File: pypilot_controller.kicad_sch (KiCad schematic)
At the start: 29 parts, among them J1 power+, J2 power-, J3 power+, J4 power+, Q1 Q_NMOS_GDS, Q2 Q_NMOS_GDS, Q3 Q_NMOS_GDS, Q4 Q_NMOS_GDS, Q5 Q_NMOS_GDS, U2 IR2101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

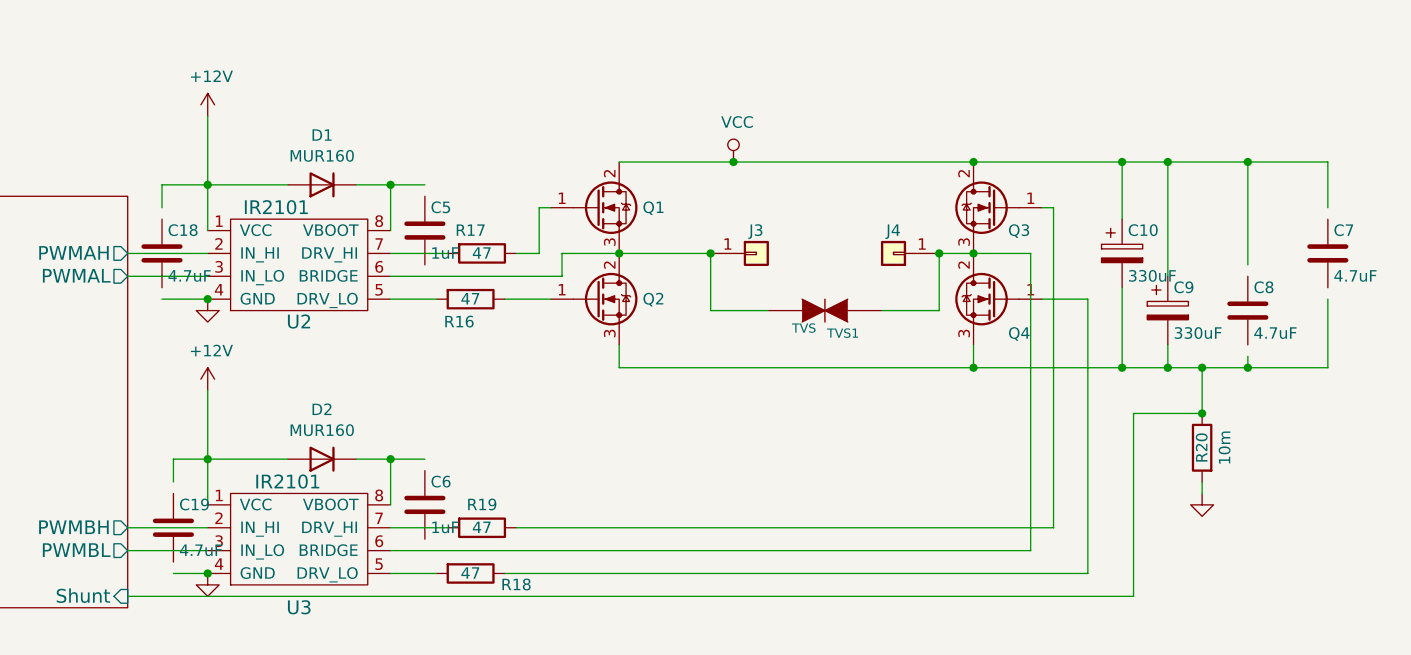
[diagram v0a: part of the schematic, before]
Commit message: Reconnect caps
Stock symbols are smaller than the Freetronics ones were
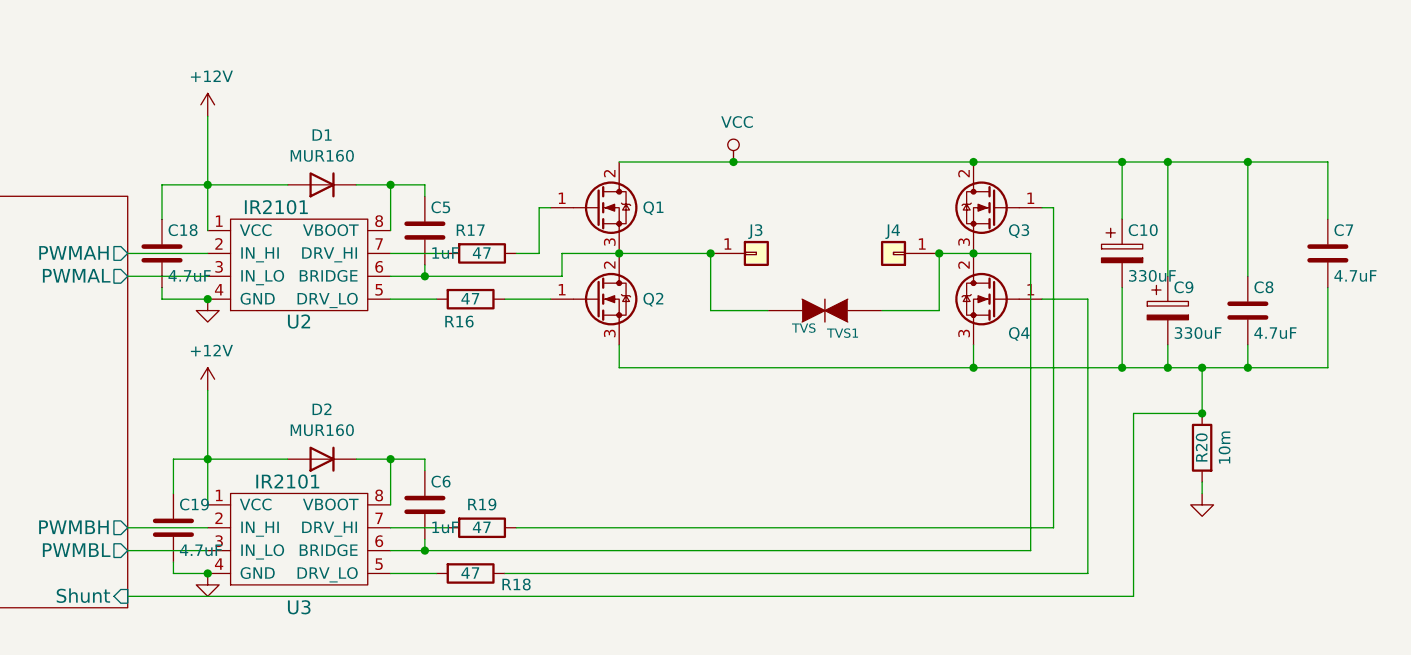
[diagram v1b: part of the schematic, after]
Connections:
- net +12V: now also C18.1, C19.1, C7.1, C8.1
- net GND: now also C18.2, C19.2
- net sense/Shunt: now also C7.2, C8.2
- net at J4.1 (Pin_1), Q3.3 (S), Q4.2 (D)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: now also C6.2
- net at J3.1 (Pin_1), Q1.3 (S), Q2.2 (D)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: now also C5.2
- net at D1.1 (K), U2.8 (VBOOT): now also C5.1
- net at D2.1 (K), U3.8 (VBOOT): now also C6.1
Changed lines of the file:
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@@
+	)
+	(junction
+		(at 152.4 113.03)
+		(diameter 0)
+		(color 0 0 0 0)
 	)
 	(junction
@@
 	)
 	(junction
+		(at 152.4 82.55)
+		(diameter 0)
+		(color 0 0 0 0)
+	)
+	(junction
 		(at 213.36 80.01)
 		(diameter 0)
@@
 	(wire
 		(pts
-			(xy 124.46 105.41) (xy 124.46 102.87)
+			(xy 124.46 102.87) (xy 124.46 106.68)
 		)
 		(stroke
@@
 	(wire
 		(pts
+			(xy 123.19 83.82) (xy 123.19 85.09)
+		)
+		(stroke
+			(width 0)
+			(type default)
+		)
+	)
+	(wire
+		(pts
 			(xy 50.8 30.48) (xy 57.15 30.48)
 		)
@@
 	(wire
 		(pts
+			(xy 252.73 83.82) (xy 252.73 92.71)
+		)
+		(stroke
+			(width 0)
+			(type default)
+		)
+	)
+	(wire
+		(pts
 			(xy 148.59 110.49) (xy 154.94 110.49)
 		)
@@
 	(wire
 		(pts
+			(xy 152.4 113.03) (xy 219.71 113.03)
+		)
+		(stroke
+			(width 0)
+			(type default)
+		)
+	)
+	(wire
+		(pts
 			(xy 124.46 115.57) (xy 128.27 115.57)
 		)
@@
 	(wire
 		(pts
-			(xy 252.73 74.93) (xy 252.73 69.85)
+			(xy 152.4 82.55) (xy 167.64 82.55)
+		)
+		(stroke
+			(width 0)
+			(type default)
+		)
+	)
+	(wire
+		(pts
+			(xy 252.73 69.85) (xy 252.73 76.2)
 		)
 		(stroke
@@
 	(wire
 		(pts
-			(xy 243.84 91.44) (xy 243.84 92.71)
+			(xy 243.84 90.17) (xy 243.84 92.71)
 		)
 		(stroke
@@
 	(wire
 		(pts
+			(xy 152.4 81.28) (xy 152.4 82.55)
+		)
+		(stroke
+			(width 0)
+			(type default)
+		)
+	)
+	(wire
+		(pts
 			(xy 60.96 90.17) (xy 63.5 90.17)
 		)
@@
 	(wire
 		(pts
-			(xy 148.59 113.03) (xy 219.71 113.03)
+			(xy 148.59 113.03) (xy 152.4 113.03)
 		)
 		(stroke
@@
 	(wire
 		(pts
+			(xy 152.4 102.87) (xy 152.4 104.14)
+		)
+		(stroke
+			(width 0)
+			(type default)
+		)
+	)
+	(wire
+		(pts
 			(xy 119.38 118.11) (xy 231.14 118.11)
 		)
@@
 	(wire
 		(pts
-			(xy 123.19 74.93) (xy 123.19 72.39)
+			(xy 123.19 72.39) (xy 123.19 76.2)
 		)
 		(stroke
@@
 	(wire
 		(pts
-			(xy 252.73 85.09) (xy 252.73 92.71)
-		)
-		(stroke
-			(width 0)
-			(type default)
-		)
-	)
-	(wire
-		(pts
 			(xy 50.8 57.15) (xy 50.8 49.53)
 		)
@@
 	(wire
 		(pts
-			(xy 148.59 82.55) (xy 167.64 82.55)
+			(xy 152.4 72.39) (xy 152.4 73.66)
+		)
+		(stroke
+			(width 0)
+			(type default)
+		)
+	)
+	(wire
+		(pts
+			(xy 148.59 82.55) (xy 152.4 82.55)
+		)
+		(stroke
+			(width 0)
+			(type default)
+		)
+	)
+	(wire
+		(pts
+			(xy 152.4 111.76) (xy 152.4 113.03)
 		)
 		(stroke
@@
 	(wire
 		(pts
-			(xy 243.84 81.28) (xy 243.84 69.85)
-		)
-		(stroke
+			(xy 243.84 69.85) (xy 243.84 82.55)
+		)
+		(stroke
+			(width 0)
+			(type default)
+		)
+	)
+	(wire
+		(pts
+			(xy 124.46 114.3) (xy 124.46 115.57)
+		)
+		(stroke

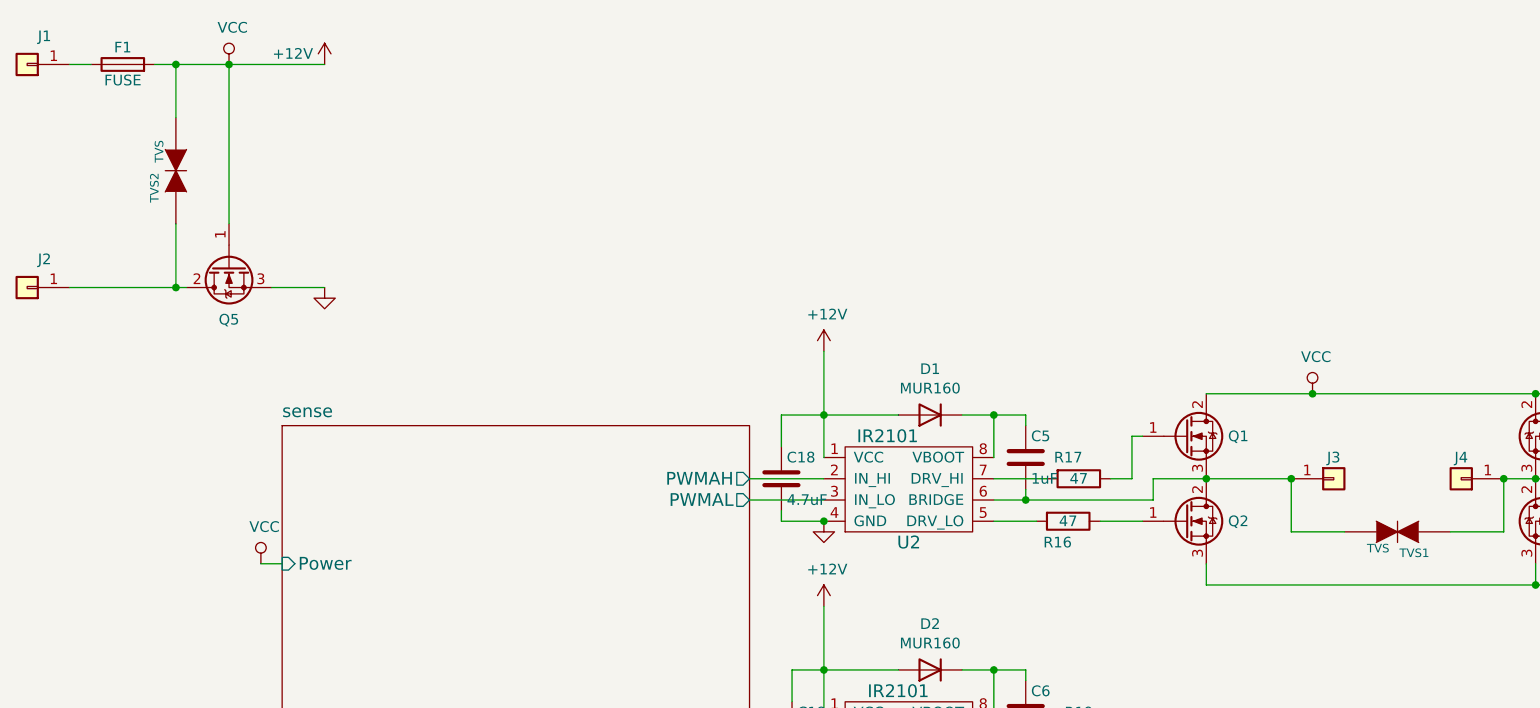
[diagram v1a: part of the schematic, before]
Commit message: Patch in particular TVS model numbers
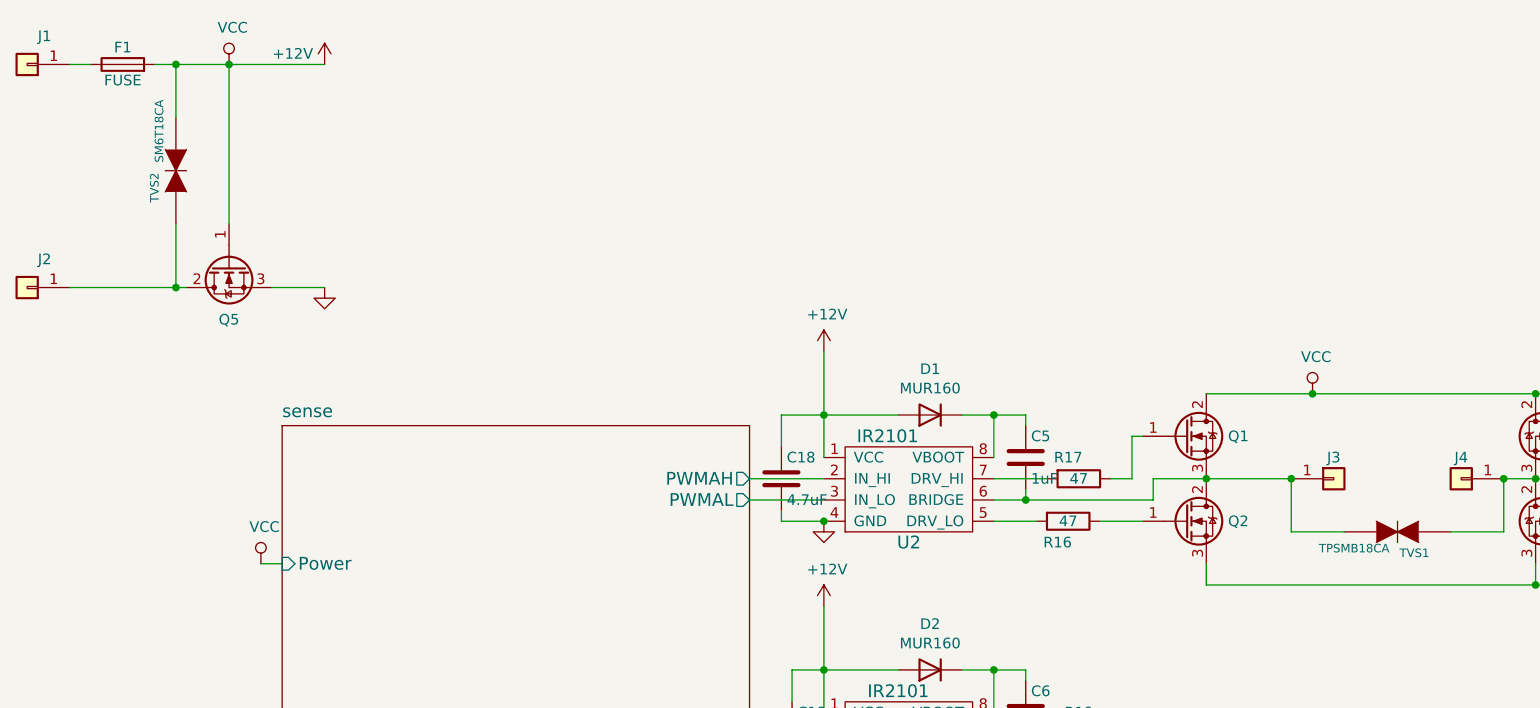
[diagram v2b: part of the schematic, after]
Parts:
- TVS1: value TVS -> TPSMB18CA
- TVS2: value TVS -> SM6T18CA
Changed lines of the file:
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@@
 			)
 		)
-		(property "Value" "TVS"
+		(property "Value" "TPSMB18CA"
 			(at 195.8848 88.3412 0)
 			(effects
@@
 			)
 		)
-		(property "Value" "TVS"
+		(property "Value" "SM6T18CA"
 			(at 48.8188 42.2148 0)
 			(effects

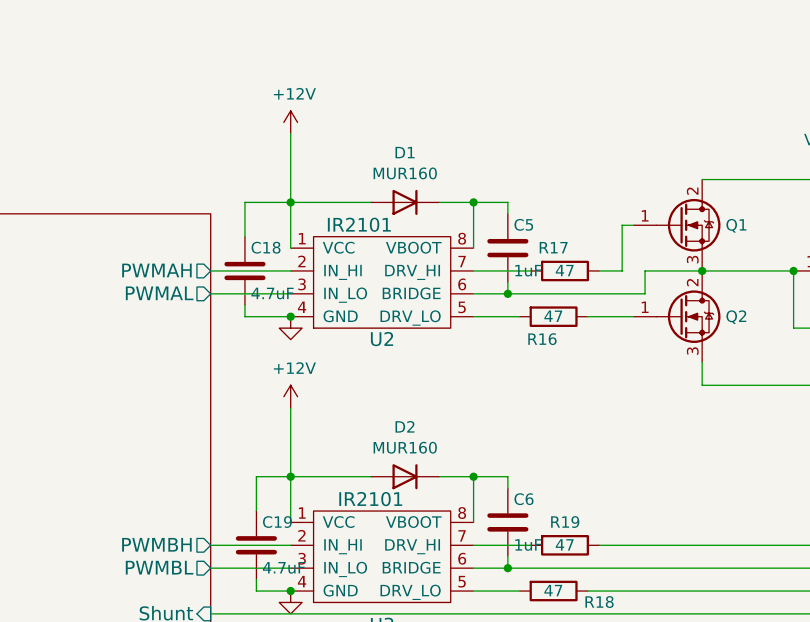
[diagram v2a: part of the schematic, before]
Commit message: Switch the charge pump diode symbol that's actually being used
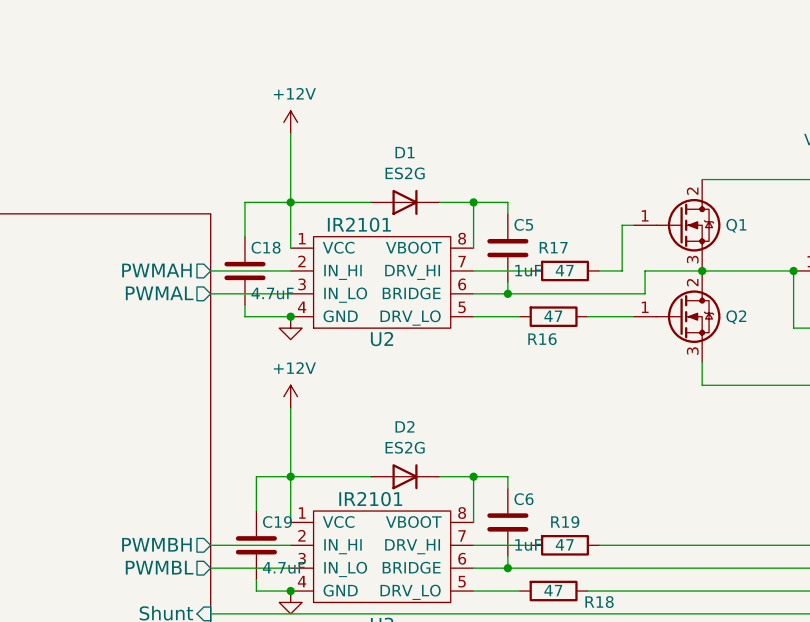
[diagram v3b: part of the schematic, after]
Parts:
- D1, D2: value MUR160 -> ES2G; symbol Diode:1N4001 -> pypilot_components:ES2G
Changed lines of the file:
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@@
 	)
 	(symbol
-		(lib_id "Diode:1N4001")
+		(lib_id "pypilot_components:ES2G")
 		(at 140.97 72.39 180)
 		(unit 1)
@@
 			)
 		)
-		(property "Value" "MUR160"
+		(property "Value" "ES2G"
 			(at 140.97 69.215 0)
 			(effects
@@
 			)
 		)
-		(property "Datasheet" "http://www.vishay.com/docs/88503/1n4001.pdf"
+		(property "Datasheet" "https://www.lcsc.com/datasheet/lcsc_datasheet_2408051407_GOODWORK-ES2G_C2848675.pdf"
 			(at 140.97 72.39 0)
 			(effects
@@
 			)
 		)
-		(property "Description" ""
+		(property "Description" "400V 2A 1.25V@6A fast recovery / high efficiency diode, SMA(DO-214AC)"
 			(at 140.97 72.39 0)
 			(effects
@@
 		)
 		(property "LCSC" "C2848675"
+			(at 140.97 72.39 0)
+			(effects
+				(font
+					(size 1.27 1.27)
+				)
+				(hide yes)
+			)
+		)
+		(property "Sim.Device" "D"
+			(at 140.97 72.39 0)
+			(effects
+				(font
+					(size 1.27 1.27)
+				)
+				(hide yes)
+			)
+		)
+		(property "Sim.Pins" "1=K 2=A"
 			(at 140.97 72.39 0)
 			(effects
@@
 	)
 	(symbol
-		(lib_id "Diode:1N4001")
+		(lib_id "pypilot_components:ES2G")
 		(at 140.97 102.87 180)
 		(unit 1)
@@
 			)
 		)
-		(property "Value" "MUR160"
+		(property "Value" "ES2G"
 			(at 140.97 99.695 0)
 			(effects
@@
 			)
 		)
-		(property "Datasheet" "http://www.vishay.com/docs/88503/1n4001.pdf"
+		(property "Datasheet" "https://www.lcsc.com/datasheet/lcsc_datasheet_2408051407_GOODWORK-ES2G_C2848675.pdf"
 			(at 140.97 102.87 0)
 			(effects
@@
 			)
 		)
-		(property "Description" ""
+		(property "Description" "400V 2A 1.25V@6A fast recovery / high efficiency diode, SMA(DO-214AC)"
 			(at 140.97 102.87 0)
 			(effects
@@
 			(at 140.97 102.87 0)
 			(effects
+				(font
+					(size 1.27 1.27)
+				)
+				(hide yes)
+			)
+		)
+		(property "Sim.Device" "D"
+			(at 140.97 102.87 0)
+			(effects
+				(font
+					(size 1.27 1.27)
+				)
+				(hide yes)
+			)
+		)
+		(property "Sim.Pins" "1=K 2=A"
+			(at 140.97 102.87 0)
+			(effects
